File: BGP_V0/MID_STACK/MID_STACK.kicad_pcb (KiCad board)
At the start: 2 copper layers, 30 x 30 mm, 11 parts, among them P1 CONN_01X05, P2 CONN_01X09, U1 OPA170

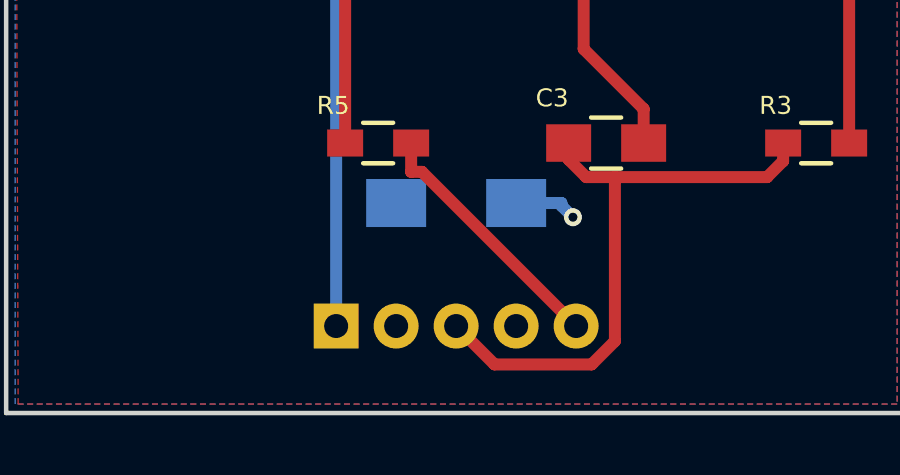
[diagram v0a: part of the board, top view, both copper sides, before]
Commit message: Gerbers
Mainly getting gerbers ready.  Issue with pots overlapping other boards in silk screens - top and bottom.
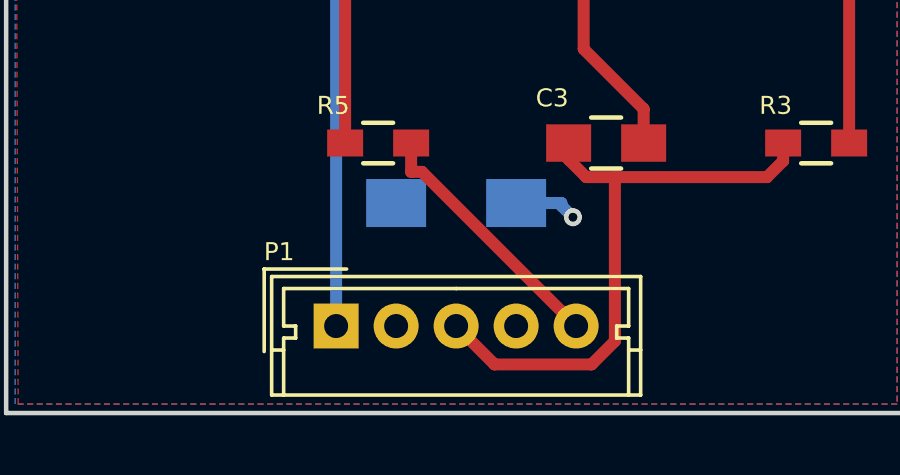
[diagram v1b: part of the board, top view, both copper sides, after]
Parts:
- P1: value CONN_01X05 -> Conn_01x05; moved to F.Cu
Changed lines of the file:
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@@
-(kicad_pcb (version 4) (host pcbnew 4.0.4-1.fc24-product)
+(kicad_pcb (version 4) (host pcbnew 4.0.7)
   (general
     (links 23)
     (no_connects 0)
-    (area 143.924999 46.424999 174.175001 95.455)
+    (area 143.924999 46.424999 174.175001 94.979999)
     (thickness 1.6)
     (drawings 9)
@@
     (pad_to_mask_clearance 0.2)
     (aux_axis_origin 0 0)
-    (visible_elements FFFFFF7F)
+    (visible_elements 7FFFFFFF)
     (pcbplotparams
       (layerselection 0x010f0_80000001)
@@
       (drillshape 0)
       (scaleselection 1)
-      (outputdirectory ../../BGP/GERBER/MID_0/))
+      (outputdirectory ../../GERBER/MID_0/))
   )
   (net 0 "")
@@
     )
   )
-  (module Connectors_Molex:Molex_MicroLatch-53253-0570_05x2.00mm_Straight (layer B.Cu)
-    (at 155 91.1)
-    (descr "Molex Micro-Latch connector, PN:53253-0570, top entry type, through hole")
-    (tags "conn molex micro latch")
-    (fp_text reference P1 (at -1.8 2.2) (layer B.SilkS)
-      (effects (font (size 0.6 0.6) (thickness 0.15)) (justify mirror))
-    )
-    (fp_text value CONN_01X05 (at 4 3.5) (layer B.Fab) hide
-      (effects (font (size 0.6 0.6) (thickness 0.15)) (justify mirror))
-    )
-    (fp_line (start -2.6 2.1) (end -2.6 -2.75) (layer B.CrtYd) (width 0.05))
-    (fp_line (start -2.6 -2.75) (end 10.55 -2.75) (layer B.CrtYd) (width 0.05))
-    (fp_line (start 10.55 -2.75) (end 10.55 2.1) (layer B.CrtYd) (width 0.05))
-    (fp_line (start 10.55 2.1) (end -2.6 2.1) (layer B.CrtYd) (width 0.05))
-    (fp_line (start -2.1 1.6) (end -2.1 -2.25) (layer B.SilkS) (width 0.15))
-    (fp_line (start -2.1 -2.25) (end 10.1 -2.25) (layer B.SilkS) (width 0.15))
-    (fp_line (start 10.1 -2.25) (end 10.1 1.6) (layer B.SilkS) (width 0.15))
-    (fp_line (start 10.1 1.6) (end -2.1 1.6) (layer B.SilkS) (width 0.15))
-    (fp_line (start 0 2) (end -0.3 2.6) (layer B.SilkS) (width 0.15))
-    (fp_line (start -0.3 2.6) (end 0.3 2.6) (layer B.SilkS) (width 0.15))
-    (fp_line (start 0.3 2.6) (end 0 2) (layer B.SilkS) (width 0.15))
-    (fp_line (start -2.1 -0.8) (end -1.7 -0.8) (layer B.SilkS) (width 0.15))
-    (fp_line (start 10.1 -0.8) (end 9.7 -0.8) (layer B.SilkS) (width 0.15))
-    (fp_line (start 4 1.2) (end -1.7 1.2) (layer B.SilkS) (width 0.15))
-    (fp_line (start -1.7 1.2) (end -1.7 0) (layer B.SilkS) (width 0.15))
-    (fp_line (start -1.7 0) (end -1.3 0) (layer B.SilkS) (width 0.15))
-    (fp_line (start -1.3 0) (end -1.3 -0.4) (layer B.SilkS) (width 0.15))
-    (fp_line (start -1.3 -0.4) (end -1.7 -0.4) (layer B.SilkS) (width 0.15))
-    (fp_line (start -1.7 -0.4) (end -1.7 -2.25) (layer B.SilkS) (width 0.15))
-    (fp_line (start 4 1.2) (end 9.7 1.2) (layer B.SilkS) (width 0.15))
-    (fp_line (start 9.7 1.2) (end 9.7 0) (layer B.SilkS) (width 0.15))
-    (fp_line (start 9.7 0) (end 9.3 0) (layer B.SilkS) (width 0.15))
-    (fp_line (start 9.3 0) (end 9.3 -0.4) (layer B.SilkS) (width 0.15))
-    (fp_line (start 9.3 -0.4) (end 9.7 -0.4) (layer B.SilkS) (width 0.15))
-    (fp_line (start 9.7 -0.4) (end 9.7 -2.25) (layer B.SilkS) (width 0.15))
-    (pad 1 thru_hole rect (at 0 0) (size 1.5 1.5) (drill 0.8) (layers *.Cu *.Mask)
-      (net 4 /IN))
-    (pad 2 thru_hole circle (at 2 0) (size 1.5 1.5) (drill 0.8) (layers *.Cu *.Mask)
-      (net 6 /V-))
-    (pad 3 thru_hole circle (at 4 0) (size 1.5 1.5) (drill 0.8) (layers *.Cu *.Mask)
-      (net 2 Earth))
-    (pad 4 thru_hole circle (at 6 0) (size 1.5 1.5) (drill 0.8) (layers *.Cu *.Mask)
-      (net 1 /V+))
-    (pad 5 thru_hole circle (at 8 0) (size 1.5 1.5) (drill 0.8) (layers *.Cu *.Mask)
-      (net 5 /OUT))
-    (model Connectors_Molex.3dshapes/Molex_MicroLatch-53253-0570_05x2.00mm_Straight.wrl
-      (at (xyz 0 0 0))
-      (scale (xyz 1 1 1))
-      (rotate (xyz 0 0 0))
-    )
-  )
   (module Capacitors_SMD:C_1206_HandSoldering (layer B.Cu)
     (at 159 87 180)
@@
     )
     (fp_text value OPA170 (at 0 2.9 270) (layer F.Fab) hide
-      (effects (font (size 1 1) (thickness 0.15)))
+      (effects (font (size 0.6 0.6) (thickness 0.15)))
     )
     (fp_text user %R (at 0 0 360) (layer F.Fab)
-      (effects (font (size 0.5 0.5) (thickness 0.075)))
+      (effects (font (size 0.6 0.6) (thickness 0.15)))
     )
     (fp_line (start -0.9 1.61) (end 0.9 1.61) (layer F.SilkS) (width 0.12))
@@
       (at (xyz 0 0 0))
       (scale (xyz 1 1 1))
+      (rotate (xyz 0 0 0))
+    )
+  )
+  (module Connectors_Molex:Molex_MicroLatch-53253-0570_05x2.00mm_Straight (layer F.Cu)
+    (at 155 91.1)
+    (descr "Molex Micro-Latch connector, PN:53253-0570, top entry type, through hole")
+    (tags "conn molex micro latch")
+    (fp_text reference P1 (at -1.9 -2.475001) (layer F.SilkS)
+      (effects (font (size 0.6 0.6) (thickness 0.15)))
+    )
+    (fp_text value Conn_01x05 (at 3.9 3.024999) (layer F.Fab) hide
+      (effects (font (size 0.6 0.6) (thickness 0.15)))
+    )
+    (fp_line (start -2 -1.5) (end -2 2.15) (layer F.Fab) (width 0.1))
+    (fp_line (start -2 2.15) (end 10 2.15) (layer F.Fab) (width 0.1))
+    (fp_line (start 10 2.15) (end 10 -1.5) (layer F.Fab) (width 0.1))
+    (fp_line (start 10 -1.5) (end -2 -1.5) (layer F.Fab) (width 0.1))
+    (fp_line (start -2.6 -2.1) (end -2.6 2.75) (layer F.CrtYd) (width 0.05))
+    (fp_line (start -2.6 2.75) (end 10.65 2.75) (layer F.CrtYd) (width 0.05))
+    (fp_line (start 10.65 2.75) (end 10.65 -2.1) (layer F.CrtYd) (width 0.05))
+    (fp_line (start 10.65 -2.1) (end -2.6 -2.1) (layer F.CrtYd) (width 0.05))
+    (fp_line (start -2.15 -1.65) (end -2.15 2.3) (layer F.SilkS) (width 0.12))
+    (fp_line (start -2.15 2.3) (end 10.15 2.3) (layer F.SilkS) (width 0.12))
+    (fp_line (start 10.15 2.3) (end 10.15 -1.65) (layer F.SilkS) (width 0.12))
+    (fp_line (start 10.15 -1.65) (end -2.15 -1.65) (layer F.SilkS) (width 0.12))
+    (fp_line (start 0.35 -1.9) (end -2.4 -1.9) (layer F.SilkS) (width 0.12))
+    (fp_line (start -2.4 -1.9) (end -2.4 0.85) (layer F.SilkS) (width 0.12))
+    (fp_line (start 0.35 -1.9) (end -2.4 -1.9) (layer F.Fab) (width 0.1))
+    (fp_line (start -2.4 -1.9) (end -2.4 0.85) (layer F.Fab) (width 0.1))
+    (fp_line (start -2.15 0.8) (end -1.75 0.8) (layer F.SilkS) (width 0.12))
+    (fp_line (start 10.15 0.8) (end 9.75 0.8) (layer F.SilkS) (width 0.12))
+    (fp_line (start 4 -1.25) (end -1.75 -1.25) (layer F.SilkS) (width 0.12))
+    (fp_line (start -1.75 -1.25) (end -1.75 0) (layer F.SilkS) (width 0.12))
+    (fp_line (start -1.75 0) (end -1.35 0) (layer F.SilkS) (width 0.12))
+    (fp_line (start -1.35 0) (end -1.35 0.4) (layer F.SilkS) (width 0.12))
+    (fp_line (start -1.35 0.4) (end -1.75 0.4) (layer F.SilkS) (width 0.12))
+    (fp_line (start -1.75 0.4) (end -1.75 2.3) (layer F.SilkS) (width 0.12))
+    (fp_line (start 4 -1.25) (end 9.75 -1.25) (layer F.SilkS) (width 0.12))
+    (fp_line (start 9.75 -1.25) (end 9.75 0) (layer F.SilkS) (width 0.12))
+    (fp_line (start 9.75 0) (end 9.35 0) (layer F.SilkS) (width 0.12))
+    (fp_line (start 9.35 0) (end 9.35 0.4) (layer F.SilkS) (width 0.12))
+    (fp_line (start 9.35 0.4) (end 9.75 0.4) (layer F.SilkS) (width 0.12))
+    (fp_line (start 9.75 0.4) (end 9.75 2.3) (layer F.SilkS) (width 0.12))
+    (fp_text user %R (at 4 1.5) (layer F.Fab) hide
+      (effects (font (size 0.6 0.6) (thickness 0.15)))
+    )
+    (pad 1 thru_hole rect (at 0 0) (size 1.5 1.5) (drill 0.8) (layers *.Cu *.Mask)
+      (net 4 /IN))
+    (pad 2 thru_hole circle (at 2 0) (size 1.5 1.5) (drill 0.8) (layers *.Cu *.Mask)
+      (net 6 /V-))
+    (pad 3 thru_hole circle (at 4 0) (size 1.5 1.5) (drill 0.8) (layers *.Cu *.Mask)
+      (net 2 Earth))
+    (pad 4 thru_hole circle (at 6 0) (size 1.5 1.5) (drill 0.8) (layers *.Cu *.Mask)
+      (net 1 /V+))
+    (pad 5 thru_hole circle (at 8 0) (size 1.5 1.5) (drill 0.8) (layers *.Cu *.Mask)
+      (net 5 /OUT))
+    (model ${KISYS3DMOD}/Connectors_Molex.3dshapes/Molex_MicroLatch-53253-0570_05x2.00mm_Straight.wrl
+      (at (xyz 0 0 0))
+      (scale (xyz 1 1 1))

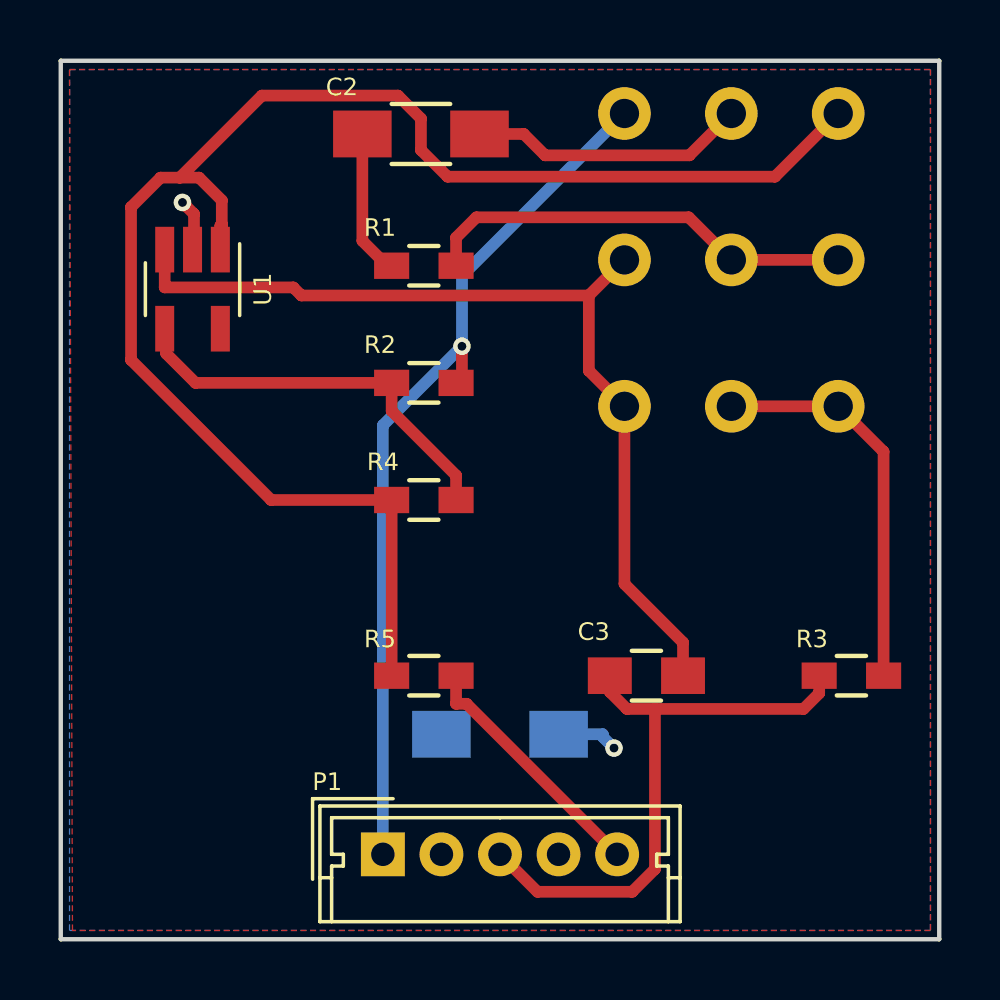
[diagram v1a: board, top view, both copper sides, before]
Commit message: Pot fixups for silkscreen overlap
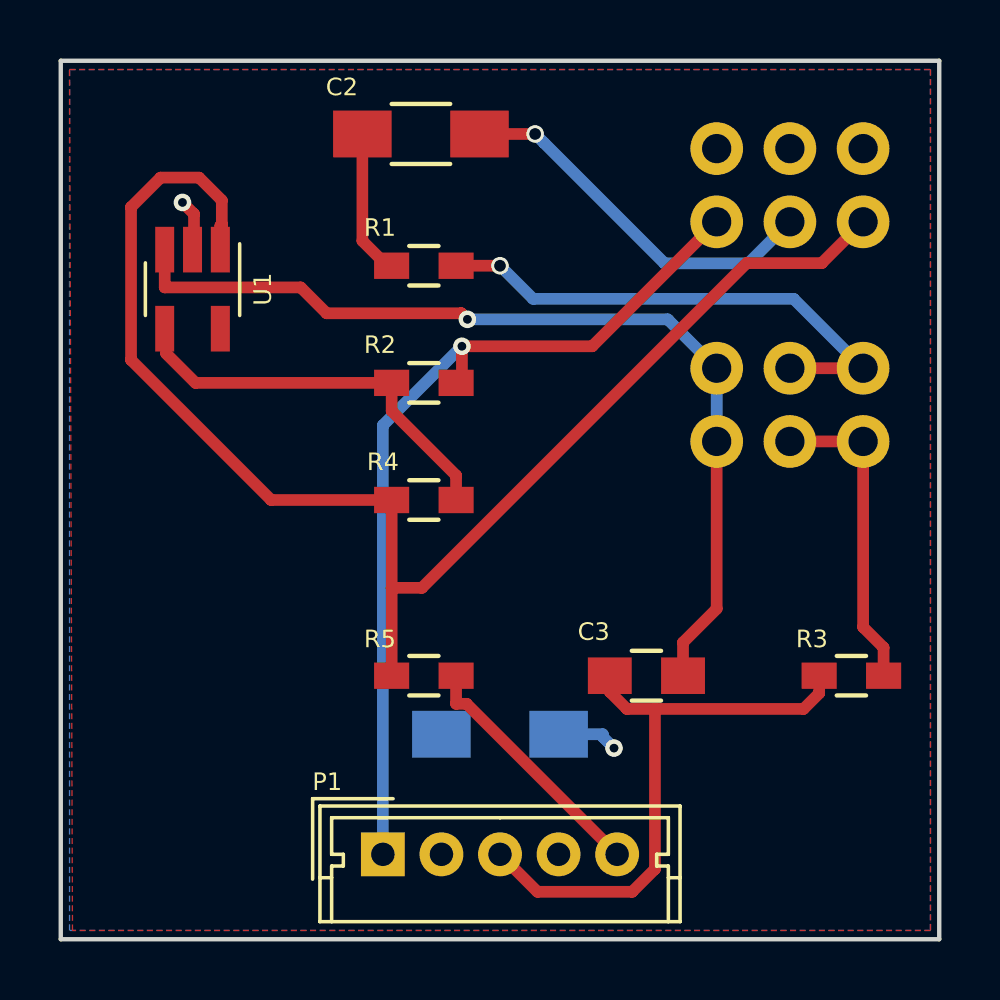
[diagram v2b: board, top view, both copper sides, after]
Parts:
- P2: value CONN_01X09 -> CONN_01X12; footprint LIBS:Potentiometer_Alpha_Tripple_Vertical_Dual_Shaft -> LIBS:Potentiometer_Alps_RK097_Quad_Vertical_Dual_Shaft
- moved P2 7.81 mm to (166.4, 67.0)
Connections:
- P2 pad 1: /IN -> Net-(P2-Pad1)
- P2 pad 2: /VOL2 -> Net-(P2-Pad2)
- P2 pad 3: /VOL3 -> Net-(P2-Pad3)
- P2 pad 4: /F1_1 -> /IN
- P2 pad 5: /F1_2 -> /VOL2
- P2 pad 6: /F1_2 -> /VOL3
- P2 pad 8: /F2_2 -> /F1_2
- P2 pad 9: /F2_2 -> /F1_2
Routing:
- net /VOL3: track 54.8 -> 49.7 mm
- net /VOL2: track 9.49 -> 13.0 mm, vias 0 -> 1
- net /F1_2: track 14.9 -> 17.8 mm, vias 0 -> 1
- net /F2_2: track 13.5 -> 10.8 mm
- net /F1_1: track 31.9 -> 32.3 mm, vias 0 -> 1

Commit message: Concentric pot fixups for 0_BT Stack and 1_HPF
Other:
- board text added: "BGP V0.0 Mid Stack"
- board text removed: "BGP V1.0 Mid Stack"
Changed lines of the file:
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@@
   (general
     (links 23)
-    (no_connects 2)
-    (area 143.924999 63.924999 174.075001 94.075001)
+    (no_connects 1)
+    (area 143.924999 63.424999 174.225001 94.979999)
     (thickness 1.6)
     (drawings 9)
@@
     )
   )
-  (gr_text "BGP V1.0\nMid Stack\n\n" (at 147.1 66.3) (layer B.SilkS)
+  (gr_text "BGP V0.0\nMid Stack\n" (at 148 66) (layer B.SilkS)
     (effects (font (size 0.6 0.6) (thickness 0.15)) (justify mirror))
   )

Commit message: V_0 Updates for caps, gerbers updated
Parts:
- C1: value 10u -> 22u
- moved C1 1.86 mm to (159.4, 85.2)
- turned U1 to 90 degrees
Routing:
- net /VOL3: track 49.7 -> 38.8 mm
- net /V+: track 2.14 -> 6.09 mm, vias 1 -> 0
- net /F1_1: track 32.3 -> 31.0 mm
